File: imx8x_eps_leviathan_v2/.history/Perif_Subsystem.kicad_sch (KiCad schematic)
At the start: 32 parts, among them CN1 DF11-16DP-2DSA(08), U13 TPS1HB08BQPWPRQ1, U14 LT8612EUDE#PBF, U15 INA260AIPWR

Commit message: Goodies
Updated USB to USB C. Added Diodes for USB. Improved Layout. Ready for some routing.
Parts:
- renumbered C32 to C31, C33 to C32, C34 to C33, C35 to C34, C36 to C35, C37 to C36, C38 to C37, C39 to C38, C40 to C39, C41 to C40, R38 to R35, R37 to R36, R39 to R37, R41 to R38, R42 to R39, R43 to R40, R44 to R41, R45 to R42, R46 to R43, R47 to R44, R48 to R45, TP23 to TP13, TP24 to TP14, TP31 to TP15, TP32 to TP16, TP33 to TP17, TP34 to TP18
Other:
- title: Leviathan V1 -> Leviathan V2

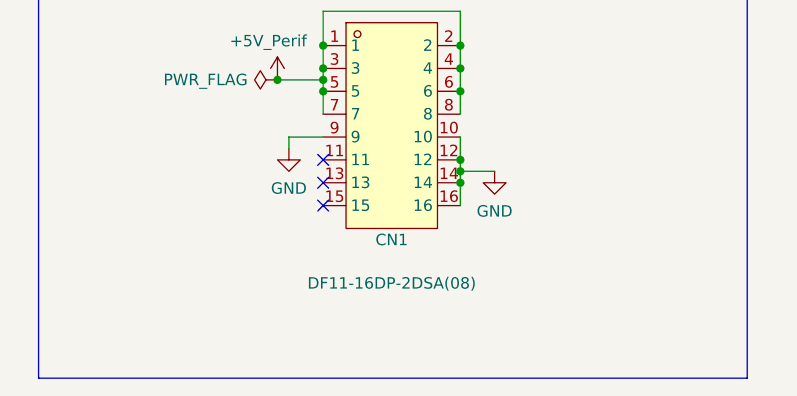
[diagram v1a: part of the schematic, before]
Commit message: Fixed an ERC error, and updated reference designators so there are no more conflicts
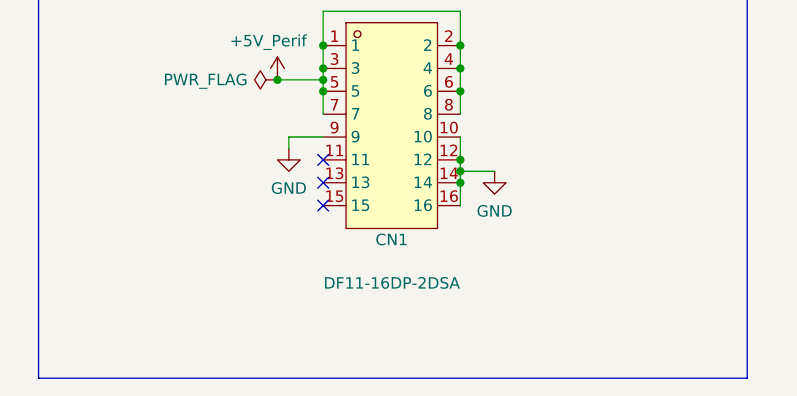
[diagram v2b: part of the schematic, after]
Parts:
- CN1: value DF11-16DP-2DSA(08) -> DF11-16DP-2DSA
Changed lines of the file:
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@@
 			)
 		)
-		(property "Value" "DF11-16DP-2DSA(08)"
+		(property "Value" "DF11-16DP-2DSA"
 			(at 54.61 157.226 0)
 			(show_name no)
